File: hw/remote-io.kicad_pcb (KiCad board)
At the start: 2 copper layers, 65 x 56.5 mm, 63 parts, among them P1 CONN_01X02, P10 CONN_01X04, P11 CONN_01X02, P2 CONN_01X08, P3 CONN_01X08, P5 CONN_02X20, Q1 DMG2305UX, Q2 DMMT5401, U1 AP1506, U2 LP2992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

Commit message: Preliminary routing of board. Messy but whatever... it's a rev 0
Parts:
- added REF**: MountingHole_2-7mm, Mounting_Holes:MountingHole_2-7mm, F.Cu at (90.5, 25.0)
- added REF**: MountingHole_2-7mm, Mounting_Holes:MountingHole_2-7mm, F.Cu at (90.5, 74.0)
- added REF**: MountingHole_2-7mm, Mounting_Holes:MountingHole_2-7mm, F.Cu at (32.5, 25.0)
- added REF**: MountingHole_2-7mm, Mounting_Holes:MountingHole_2-7mm, F.Cu at (32.5, 74.0)
- R27, R28: moved to F.Cu
- moved C12 27.2 mm to (54.2, 55.9)
- moved R27 25.2 mm to (61.4, 57.9), turned to 180 degrees
- moved R28 23.6 mm to (61.4, 55.0), turned to 0 degrees
- moved R23 8.60 mm to (35.6, 56.8)
- moved C10 6.52 mm to (76.8, 51.9), turned to 270 degrees
- moved C11 6.27 mm to (76.8, 59.1), turned to 90 degrees
- moved D2 3.64 mm to (35.6, 45.4)
- moved D3 3.64 mm to (35.6, 48.1)
- moved D4 3.64 mm to (35.6, 50.8)
- moved R2 3.64 mm to (35.6, 45.4)
- moved R3 3.64 mm to (35.6, 48.1)
- moved D1 3.64 mm to (35.6, 42.8)
- moved R1 3.64 mm to (35.6, 42.8)
- moved R4 3.60 mm to (35.6, 50.8)
- moved C13 2.67 mm to (75.7, 67.0), turned to 180 degrees
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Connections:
- U1 pad 3: Net-(U1-Pad3) -> GND
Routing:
- net +3V3: track 9.75 -> 107.3 mm, vias 2 -> 6
- net /CAN Controller and Transceiver/CAN_~CS: track 0.00 -> 74.3 mm, vias 0 -> 2
- net /LED3: track 0.00 -> 73.8 mm, vias 0 -> 7
- net /LED2: track 0.00 -> 70.7 mm, vias 0 -> 3
- net /LED1: track 0.00 -> 70.4 mm, vias 0 -> 1
- net /I2C ID EEPROM/ID_SC: track 0.00 -> 69.6 mm, vias 0 -> 2
- net /Battery Monitor/ADC_CLK: track 0.00 -> 66.0 mm, vias 0 -> 2
- net /Battery Monitor/ADC_DIN: track 0.00 -> 63.0 mm, vias 0 -> 3
- net /LED0: track 1.57 -> 62.2 mm, vias 1 -> 0
- net /Battery Monitor/ADC_DOUT: track 0.00 -> 59.8 mm, vias 0 -> 2
- net /Battery Monitor/ADC_~CS~/SHDN: track 0.19 -> 59.7 mm, vias 0 -> 3
- net /CAN Controller and Transceiver/CAN_VSENSE: track 0.00 -> 53.4 mm, vias 0 -> 1
- net /SW_IN3: track 0.00 -> 53.2 mm
- net /I2C ID EEPROM/ID_SD: track 0.00 -> 53.0 mm, vias 0 -> 3
- net /CAN Controller and Transceiver/CAN_~INT: track 0.00 -> 46.6 mm, vias 0 -> 3
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- added copper zone on B.Cu, net GND
- added copper zone on F.Cu, net GND
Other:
- net class Default: clearance 0.0254 -> 0.075
- rule trace_clearance: 0.0254 -> 0.075

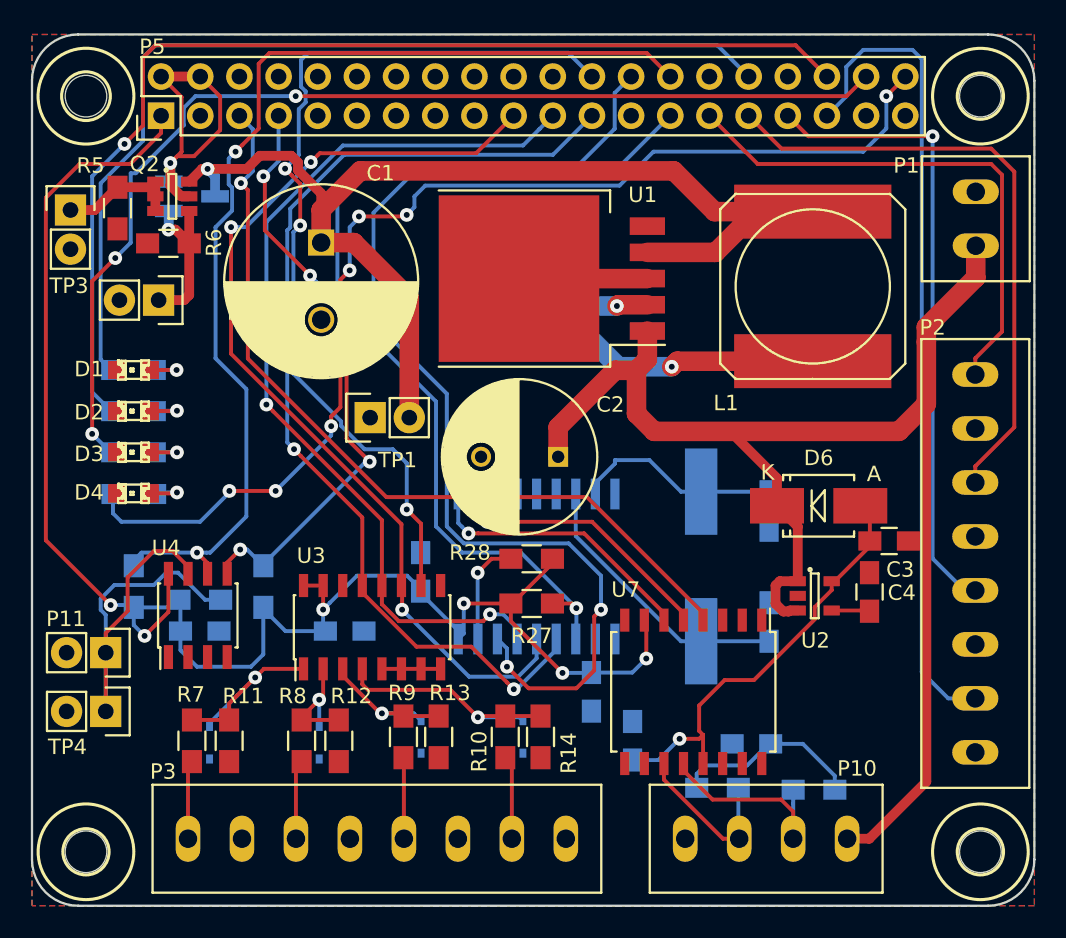
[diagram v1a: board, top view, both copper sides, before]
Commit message: Isolated CAN bus connections and added proper mounting holes
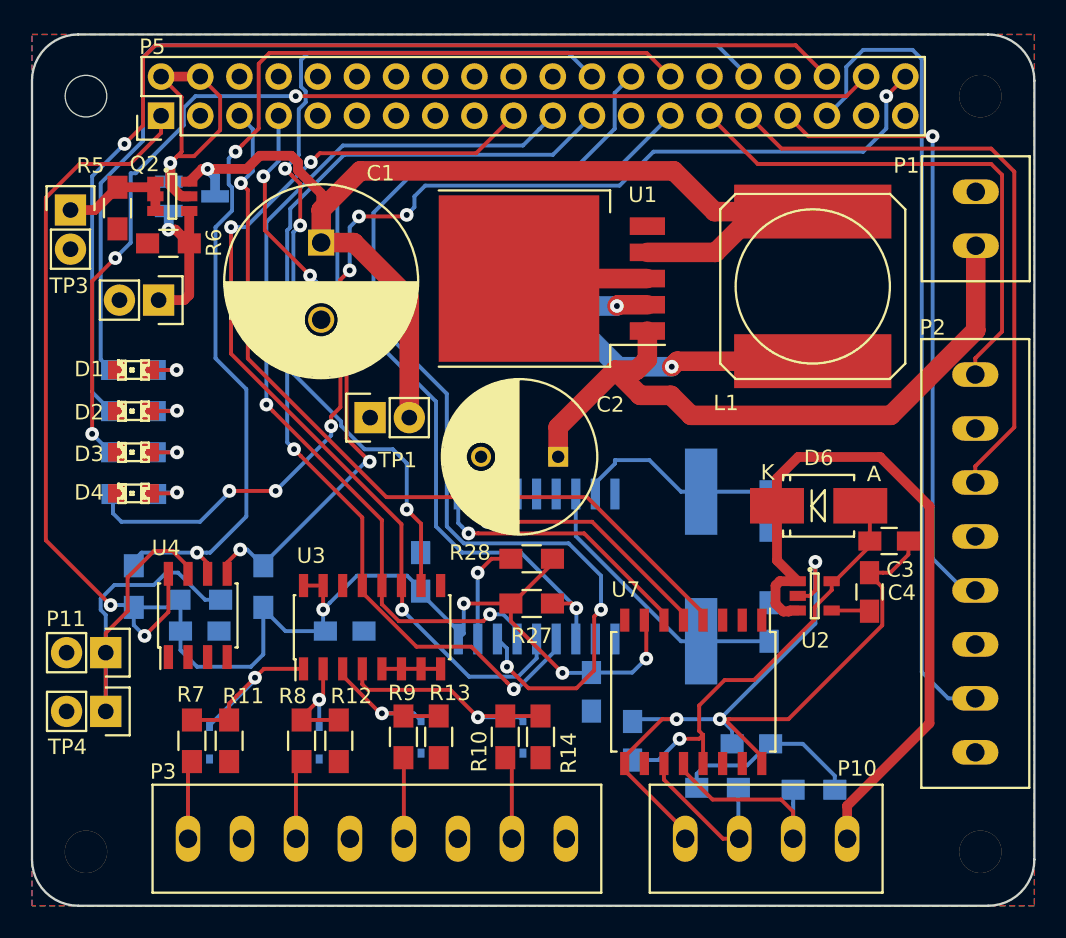
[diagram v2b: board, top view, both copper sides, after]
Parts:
- removed REF** (x4): MountingHole_2-7mm, Mounting_Holes:MountingHole_2-7mm
- added H1: MOUNT_HOLE, Mounting_Holes:MountingHole_2-7mm, F.Cu at (32.5, 25.0)
- added H2: MOUNT_HOLE, Mounting_Holes:MountingHole_2-7mm, F.Cu at (90.5, 25.0)
- added H3: MOUNT_HOLE, Mounting_Holes:MountingHole_2-7mm, F.Cu at (90.5, 74.0)
- added H4: MOUNT_HOLE, Mounting_Holes:MountingHole_2-7mm, F.Cu at (32.5, 74.0)
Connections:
- C13 pad 2: GND -> GNDA
- C3 pad 2: GND -> GNDA
- C4 pad 2: GND -> GNDA
- C9 pad 2: GND -> GNDA
- D6 pad 1: +12V -> +12VA
- P10 pad 1: +12V -> +12VA
- P10 pad 4: GND -> GNDA
- U1 pad 3: GND -> Net-(U1-Pad3)
- U2 pad 1: +12V -> +12VA
- U2 pad 2: GND -> GNDA
- U2 pad 3: +12V -> +12VA
- U7 pad 16: GND -> GNDA
- U7 pad 9: GND -> GNDA
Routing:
- net GNDA: track 0.00 -> 59.8 mm, vias 0 -> 3
- net +12V: track 97.8 -> 43.7 mm
- net +12VA: track 0.00 -> 47.2 mm
- net Net-(U1-Pad3): track 0.00 -> 8.32 mm
- net GND: track 12.1 -> 3.81 mm
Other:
- board text added: "12**"
- board text added: "12V_IN"
- board text added: "BAT_MEAS"
- board text added: "CAN"
- board text added: "G"
- board text added: "G**"
- board text added: "GND"
- board text added: "H"
- board text added: "L"
- board text added: "SWITCHES"

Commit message: Finished rev 0 with gerbers and drills
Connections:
- P5 pad 17: +3V3 -> (no net)
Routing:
- net GND: track 3.81 -> 44.9 mm, vias 0 -> 5
- net Net-(P11-Pad1): track 31.4 -> 29.9 mm
- net GNDA: track 59.8 -> 61.2 mm
- net /CAN Controller and Transceiver/CAN_~CS: track 74.3 -> 72.9 mm
- net +3V3: track 107.3 -> 108.4 mm
- net +5VA: track 28.1 -> 29.1 mm
- net /Battery Monitor/ADC_DIN: track 63.0 -> 63.6 mm
- net +12V: track 43.7 -> 44.3 mm
- net /Battery Monitor/ADC_~CS~/SHDN: track 59.7 -> 59.2 mm
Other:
- net class Default: clearance 0.075 -> 0.1524
- rule trace_clearance: 0.075 -> 0.1524
- rule trace_min: 0.254 -> 0.1524
